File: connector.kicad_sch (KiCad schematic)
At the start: 4 parts, among them J1 Screw_Terminal_01x04

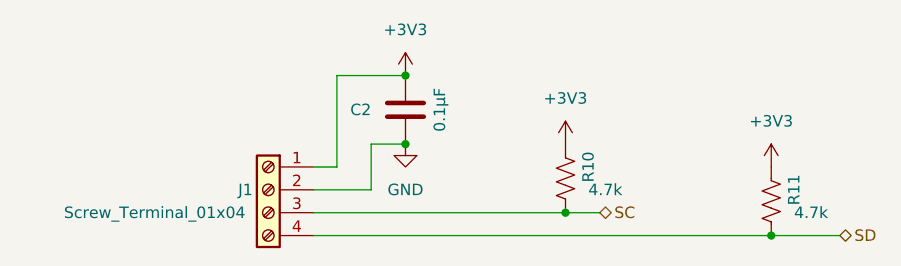
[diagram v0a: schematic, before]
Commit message: changed single 10k pull-up to 4.7k like others. Renumbered components to fill numbering gaps.
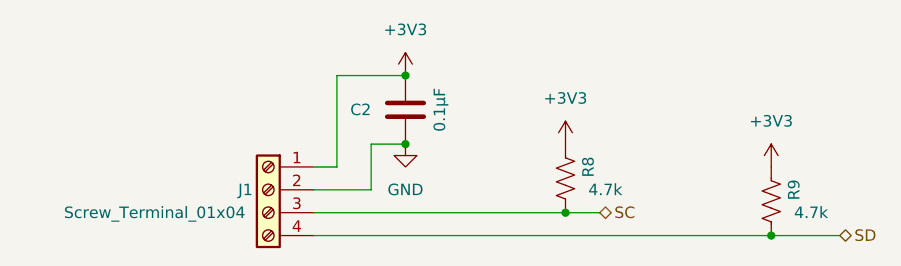
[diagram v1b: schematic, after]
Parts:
- renumbered R10 to R8, R11 to R9
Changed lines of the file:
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@@
 		(dnp no)
 		(fields_autoplaced yes)
-		(property "Reference" "R10"
+		(property "Reference" "R8"
 			(at 105.41 41.91 90)
 			(effects
@@
 			(project "multiplexI2CwithRJ11"
 				(path "/0c2d0c14-8850-4a30-bb78-b2f40cb442ba/24b4e8ef-9825-49f5-9404-579a6ea7b19b"
+					(reference "R16")
+					(unit 1)
+				)
+				(path "/0c2d0c14-8850-4a30-bb78-b2f40cb442ba/8a12c970-6e82-4f99-ab8e-e5d673f5e8d9"
+					(reference "R10")
+					(unit 1)
+				)
+				(path "/0c2d0c14-8850-4a30-bb78-b2f40cb442ba/e657843b-000b-4d7c-a001-36698309a032"
+					(reference "R8")
+					(unit 1)
+				)
+				(path "/0c2d0c14-8850-4a30-bb78-b2f40cb442ba/f2b2a76e-3be2-4491-ad7e-06b9b1e9bf9c"
 					(reference "R18")
-					(unit 1)
-				)
-				(path "/0c2d0c14-8850-4a30-bb78-b2f40cb442ba/8a12c970-6e82-4f99-ab8e-e5d673f5e8d9"
-					(reference "R12")
-					(unit 1)
-				)
-				(path "/0c2d0c14-8850-4a30-bb78-b2f40cb442ba/e657843b-000b-4d7c-a001-36698309a032"
-					(reference "R10")
-					(unit 1)
-				)
-				(path "/0c2d0c14-8850-4a30-bb78-b2f40cb442ba/f2b2a76e-3be2-4491-ad7e-06b9b1e9bf9c"
-					(reference "R20")
 					(unit 1)
 				)
@@
 		(dnp no)
 		(fields_autoplaced yes)
-		(property "Reference" "R11"
+		(property "Reference" "R9"
 			(at 128.27 44.45 90)
 			(effects
@@
 			(project "multiplexI2CwithRJ11"
 				(path "/0c2d0c14-8850-4a30-bb78-b2f40cb442ba/24b4e8ef-9825-49f5-9404-579a6ea7b19b"
+					(reference "R17")
+					(unit 1)
+				)
+				(path "/0c2d0c14-8850-4a30-bb78-b2f40cb442ba/8a12c970-6e82-4f99-ab8e-e5d673f5e8d9"
+					(reference "R11")
+					(unit 1)
+				)
+				(path "/0c2d0c14-8850-4a30-bb78-b2f40cb442ba/e657843b-000b-4d7c-a001-36698309a032"
+					(reference "R9")
+					(unit 1)
+				)
+				(path "/0c2d0c14-8850-4a30-bb78-b2f40cb442ba/f2b2a76e-3be2-4491-ad7e-06b9b1e9bf9c"
 					(reference "R19")
 					(unit 1)
 				)
-				(path "/0c2d0c14-8850-4a30-bb78-b2f40cb442ba/8a12c970-6e82-4f99-ab8e-e5d673f5e8d9"
-					(reference "R13")
-					(unit 1)
-				)
-				(path "/0c2d0c14-8850-4a30-bb78-b2f40cb442ba/e657843b-000b-4d7c-a001-36698309a032"
-					(reference "R11")
-					(unit 1)
-				)
-				(path "/0c2d0c14-8850-4a30-bb78-b2f40cb442ba/f2b2a76e-3be2-4491-ad7e-06b9b1e9bf9c"
-					(reference "R21")
-					(unit 1)
-				)

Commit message: cleaned up fab layer annotation.
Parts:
- C2, R8, R9: Notes (none) -> or equivalent
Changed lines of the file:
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@@
 			)
 		)
-		(property "Notes" ""
+		(property "Notes" "or equivalent"
 			(at 102.87 43.18 0)
+			(effects
+				(font
+					(size 1.27 1.27)
+				)
+				(hide yes)
+			)
+		)
+		(property "Manuf Part" ""
+			(at 102.87 43.18 90)
+			(effects
+				(font
+					(size 1.27 1.27)
+				)
+				(hide yes)
+			)
+		)
+		(property "Manuf Series" ""
+			(at 102.87 43.18 90)
 			(effects
 				(font
@@
 			)
 		)
-		(property "Notes" ""
+		(property "Notes" "or equivalent"
 			(at 125.73 45.72 0)
+			(effects
+				(font
+					(size 1.27 1.27)
+				)
+				(hide yes)
+			)
+		)
+		(property "Manuf Part" ""
+			(at 125.73 45.72 90)
+			(effects
+				(font
+					(size 1.27 1.27)
+				)
+				(hide yes)
+			)
+		)
+		(property "Manuf Series" ""
+			(at 125.73 45.72 90)
 			(effects
 				(font
@@
 			)
 		)
-		(property "Notes" ""
+		(property "Notes" "or equivalent"
+			(at 85.09 35.56 0)
+			(effects
+				(font
+					(size 1.27 1.27)
+				)
+				(hide yes)
+			)
+		)
+		(property "Manuf Part" ""
+			(at 85.09 35.56 0)
+			(effects
+				(font
+					(size 1.27 1.27)
+				)
+				(hide yes)
+			)
+		)
+		(property "Manuf Series" ""
 			(at 85.09 35.56 0)
 			(effects
@@
 			(at 69.85 44.45 0)
 			(effects
+				(font
+					(size 1.27 1.27)
+				)
+				(hide yes)
+			)
+		)
+		(property "Manuf Part" ""
+			(at 69.85 44.45 0)
+			(effects
+				(font
+					(size 1.27 1.27)
+				)
+				(hide yes)
+			)
+		)
+		(property "Manuf Series" ""
+			(at 69.85 44.45 0)
+			(effects

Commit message: ongoing.
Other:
- title: Multiplex I2C to Screw Terminal connectors -> Screw Terminal connector
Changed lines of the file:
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@@
 	(paper "A4")
 	(title_block
-		(title "Multiplex I2C to Screw Terminal connectors")
-		(date "2025-09-07")
-		(rev "v0.2.0")
+		(title "Screw Terminal connector")
+		(date "2025-11-29")
+		(rev "v0.2.2")
 	)
 	(junction

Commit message: ongoing cleanup for submit.
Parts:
- C2: Package (none) -> C_0402_1005Metric
- J1: Package (none) -> 1x04_P2.54mm_Horizontal
- R8, R9: Package (none) -> R_0402_1005Metric
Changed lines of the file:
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@@
 			)
 		)
-		(property "Datasheet" "~"
+		(property "Datasheet" ""
 			(at 102.87 43.18 0)
 			(effects
@@
 		)
 		(property "Manuf Series" ""
+			(at 102.87 43.18 90)
+			(effects
+				(font
+					(size 1.27 1.27)
+				)
+				(hide yes)
+			)
+		)
+		(property "Package" "R_0402_1005Metric"
 			(at 102.87 43.18 90)
 			(effects
@@
 			)
 		)
-		(property "Datasheet" "~"
+		(property "Datasheet" ""
 			(at 125.73 45.72 0)
 			(effects
@@
 		)
 		(property "Manuf Series" ""
+			(at 125.73 45.72 90)
+			(effects
+				(font
+					(size 1.27 1.27)
+				)
+				(hide yes)
+			)
+		)
+		(property "Package" "R_0402_1005Metric"
 			(at 125.73 45.72 90)
 			(effects
@@
 			)
 		)
-		(property "Datasheet" "~"
+		(property "Datasheet" ""
 			(at 85.09 35.56 0)
 			(effects
@@
 		)
 		(property "Manuf Series" ""
+			(at 85.09 35.56 0)
+			(effects
+				(font
+					(size 1.27 1.27)
+				)
+				(hide yes)
+			)
+		)
+		(property "Package" "C_0402_1005Metric"
 			(at 85.09 35.56 0)
 			(effects
@@
 			)
 		)
-		(property "Datasheet" "~"
-			(at 69.85 44.45 0)
-			(effects
-				(font
-					(size 1.27 1.27)
-				)
-				(hide yes)
-			)
-		)
-		(property "Description" "Generic screw terminal, single row, 01x04, script generated (kicad-library-utils/schlib/autogen/connector/)"
+		(property "Datasheet" "https://www.lcsc.com/datasheet/C474920.pdf"
+			(at 69.85 44.45 0)
+			(effects
+				(font
+					(size 1.27 1.27)
+				)
+				(hide yes)
+			)
+		)
+		(property "Description" "Generic screw terminal, single row, 01x04"
 			(at 69.85 44.45 0)
 			(effects
@@
 			(at 69.85 44.45 0)
 			(effects
+				(font
+					(size 1.27 1.27)
+				)
+				(hide yes)
+			)
+		)
+		(property "Package" "1x04_P2.54mm_Horizontal"
+			(at 69.85 44.45 0)
+			(effects
